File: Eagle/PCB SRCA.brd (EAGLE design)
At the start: 160 x 100 mm, 81 parts, among them IC1 DSPIC30F4011-30I_P, IC2 LM324LVIDR, IC3 LM35DZ_NOPB, IC4 FT232RL-REEL, J1 TBL002A-350-03GR-2OR, J2 TBL002A-350-03GR-2OR, J3 TBL002A-350-03GR-2OR, J4 44914-0801, J5 TBL002A-350-03GR-2OR, J6 44914-0401, Q1 TIP41C, T1 2N3904, T10 2N3904, T11 2N3904, T2 2N3904, T3 2N3904, T4 2N3904, T5 2N3904, T6 2N3904, T7 2N3904, T8 2N3904, T9 2N3904, U1 LD1117S33TR

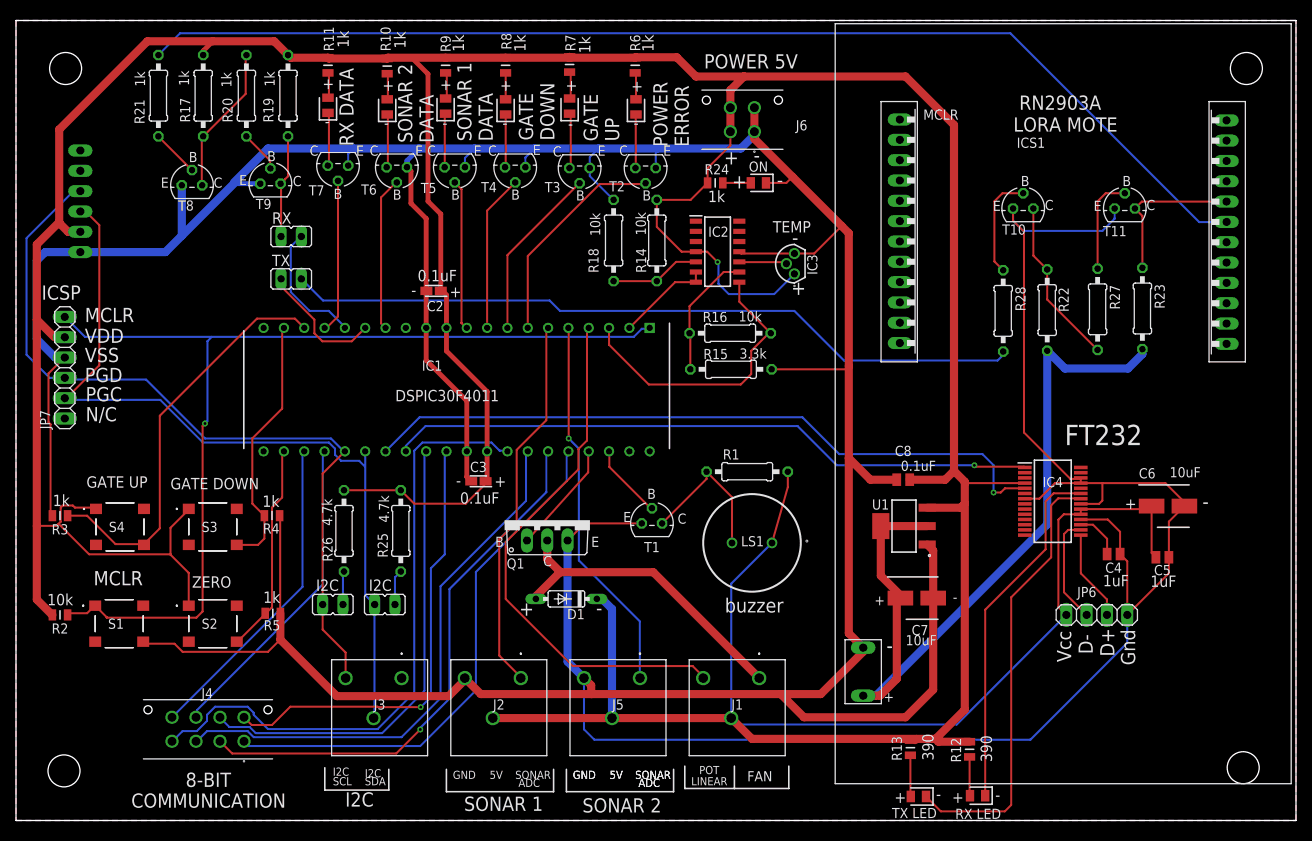
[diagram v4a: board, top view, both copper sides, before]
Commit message: 06-09-2021
se revirtio el cambio de el divisor de voltaje del lora al DSPIC
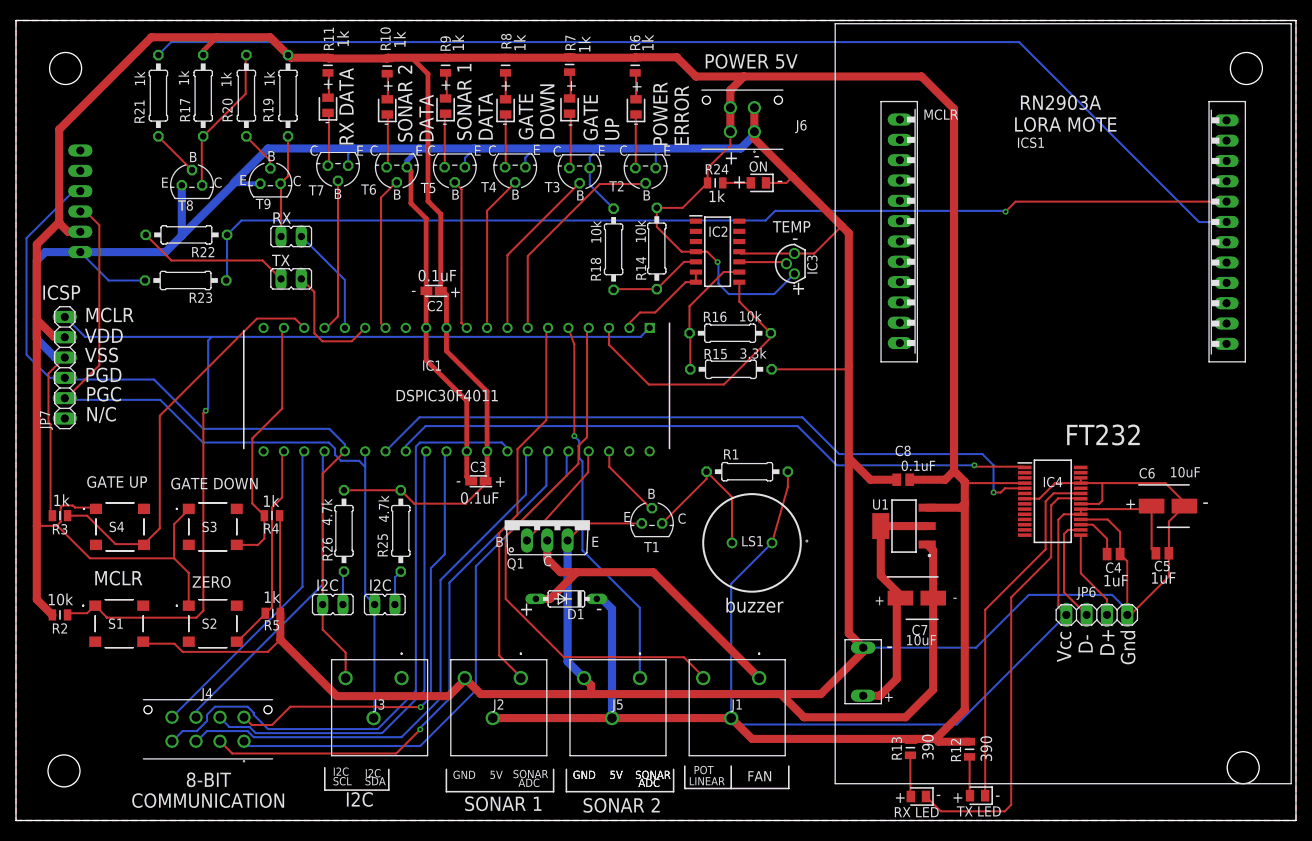
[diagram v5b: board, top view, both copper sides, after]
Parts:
- removed R27, R28: 1k, rcl:0207/10
- removed T10, T11: 2N3904, transistor-neu-to92:TO92
- R22: value 1k -> 3.3k
- R23: value 1k -> 6.8k
- moved R23 119.7 mm to (21.2, 67.5), turned to 180 degrees
- moved R22 108.0 mm to (21.3, 73.2), turned to 180 degrees
- moved R18 1.10 mm to (74.7, 71.4)
- moved R14 1.00 mm to (80.1, 71.5)
- moved C5 0.50 mm to (143.3, 33.4)
- turned JP2 to 90 degrees
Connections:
- removed net N$29: JP2.2, R28.2
- removed net N$33: R28.1, T10.2
- removed net N$34: R27.1, T11.2
- net 3.3V: no longer R22.2, R23.2
- net GND: now also R23.2; no longer T10.3, T11.3
- net N$27: now also JP2.2, R22.2; no longer R22.1, R27.2, T10.1
- net RX_LORA: now also R22.1; no longer T11.1
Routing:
- net RX_LORA: track 19.6 -> 132.5 mm, vias 0 -> 1
- net N$29: track 92.7 -> 0.00 mm
- net GND: track 698.0 -> 607.9 mm
- net 3.3V: track 98.9 -> 31.2 mm
- net N$33: track 13.1 -> 0.00 mm
- net N$34: track 12.2 -> 0.00 mm
- net RX_UART: track 16.2 -> 13.7 mm
- net FAN1: track 39.6 -> 41.5 mm
- net N$27: track 21.0 -> 19.2 mm
- net V+: track 649.5 -> 651.1 mm
- net TEMP: track 36.7 -> 35.4 mm
- net TX_UART: track 16.0 -> 14.9 mm
- net TX_LORA: track 144.4 -> 143.5 mm
- net I2C_SCL: track 99.2 -> 99.7 mm

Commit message: 06/09/2021
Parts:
- removed C8: C0805X104K1RAC3316, C0805X104K1RAC3316:CAPC2012X100N
- added C1: TAJR104K020RNJ, TAJR104K020RNJ:CAPPM2014X120N
- C3: value TAJR104K020RNJ -> C0805X104K1RAC3316; device TAJR104K020RNJ:CAPPM2014X120N -> C0805X104K1RAC3316:CAPC2012X100N
- C5: value C0805X104K1RAC3316 -> UUP1C100MCL1GS; device C0805X104K1RAC3316:CAPC2012X100N -> UUP1C100MCL1GS:CAPAE530X610N
- C6: value UUP1C100MCL1GS -> C0805X104K1RAC3316; device UUP1C100MCL1GS:CAPAE530X610N -> C0805X104K1RAC3316:CAPC2012X100N
- moved C3 86.0 mm to (143.3, 33.4)
- moved C6 33.3 mm to (110.9, 42.6), turned to 180 degrees
- moved C2 24.4 mm to (57.8, 42.4)
- moved C5 5.94 mm to (144.0, 39.3), turned to 0 degrees
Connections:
- net GND: now also C1.2, C3.1, C5.2; no longer C3.2, C5.1, C8.2
- net V+: now also C1.1, C3.2, C5.1; no longer C3.1, C5.2, C8.1
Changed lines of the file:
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@@
 <drawing>
 <settings>
-<setting alwaysvectorfont="yes"/>
+<setting alwaysvectorfont="no"/>
 <setting verticaltext="up"/>
 </settings>
@@
 <attribute name="NAME" x="87.8" y="73.6" size="1.27" layer="25" align="center"/>
 </element>
-<element name="C2" library="TAJR104K020RNJ" library_urn="urn:adsk.eagle:library:30514861" package="CAPPM2014X120N" package3d_urn="urn:adsk.eagle:package:30514864/2" value="TAJR104K020RNJ" x="52.2" y="66.2" smashed="yes" rot="R180">
+<element name="C1" library="TAJR104K020RNJ" library_urn="urn:adsk.eagle:library:30514861" package="CAPPM2014X120N" package3d_urn="urn:adsk.eagle:package:30514864/2" value="TAJR104K020RNJ" x="52.2" y="66.2" smashed="yes" rot="R180">
 <attribute name="DESCRIPTION" value="TAJ smt tant capacitor,case R,0.1uF,20V AVX 100nF SMD Solid MnO2 Tantalum Electrolytic Capacitor, 20 V dc +/-10%, TAJ Series" x="52.2" y="66.2" size="1.778" layer="27" rot="R180" display="off"/>
 <attribute name="HEIGHT" value="1.2mm" x="52.2" y="66.2" size="1.778" layer="27" rot="R180" display="off"/>
@@
 <attribute name="NAME" x="52.4" y="64.3" size="1.27" layer="25" rot="R180" align="center"/>
 </element>
-<element name="C3" library="TAJR104K020RNJ" library_urn="urn:adsk.eagle:library:30514861" package="CAPPM2014X120N" package3d_urn="urn:adsk.eagle:package:30514864/2" value="TAJR104K020RNJ" x="57.8" y="42.4" smashed="yes" rot="R180">
+<element name="C2" library="TAJR104K020RNJ" library_urn="urn:adsk.eagle:library:30514861" package="CAPPM2014X120N" package3d_urn="urn:adsk.eagle:package:30514864/2" value="TAJR104K020RNJ" x="57.8" y="42.4" smashed="yes" rot="R180">
 <attribute name="DESCRIPTION" value="TAJ smt tant capacitor,case R,0.1uF,20V AVX 100nF SMD Solid MnO2 Tantalum Electrolytic Capacitor, 20 V dc +/-10%, TAJ Series" x="57.8" y="42.4" size="1.778" layer="27" rot="R180" display="off"/>
 <attribute name="HEIGHT" value="1.2mm" x="57.8" y="42.4" size="1.778" layer="27" rot="R180" display="off"/>
@@
 <attribute name="VALUE" x="39.535" y="36.8394" size="1.27" layer="25" ratio="10" rot="R90"/>
 </element>
-<element name="C5" library="C0805X104K1RAC3316" library_urn="urn:adsk.eagle:library:30534331" package="CAPC2012X100N" package3d_urn="urn:adsk.eagle:package:30534334/2" value="C0805X104K1RAC3316" x="143.3" y="33.4" smashed="yes" rot="R180">
+<element name="C3" library="C0805X104K1RAC3316" library_urn="urn:adsk.eagle:library:30534331" package="CAPC2012X100N" package3d_urn="urn:adsk.eagle:package:30534334/2" value="C0805X104K1RAC3316" x="143.3" y="33.4" smashed="yes" rot="R180">
 <attribute name="DESCRIPTION" value="Multilayer Ceramic Capacitors MLCC - SMD/SMT 100V .1uF X7R AUTO 5mm Flex VW80808" x="143.3" y="33.4" size="1.778" layer="27" rot="R180" display="off"/>
 <attribute name="HEIGHT" value="1mm" x="143.3" y="33.4" size="1.778" layer="27" rot="R180" display="off"/>
@@
 <attribute name="NAME" x="129.6" y="42.3" size="1.27" layer="25" align="center"/>
 </element>
-<element name="C6" library="UUP1C100MCL1GS" library_urn="urn:adsk.eagle:library:30514850" package="CAPAE530X610N" package3d_urn="urn:adsk.eagle:package:30514853/2" value="UUP1C100MCL1GS" x="144" y="39.3" smashed="yes">
+<element name="C5" library="UUP1C100MCL1GS" library_urn="urn:adsk.eagle:library:30514850" package="CAPAE530X610N" package3d_urn="urn:adsk.eagle:package:30514853/2" value="UUP1C100MCL1GS" x="144" y="39.3" smashed="yes">
 <attribute name="DESCRIPTION" value="Aluminum Electrolytic Capacitors - SMD 16volts 10uF AEC-Q200" x="144" y="39.3" size="1.778" layer="27" display="off"/>
 <attribute name="HEIGHT" value="6.1mm" x="144" y="39.3" size="1.778" layer="27" display="off"/>
@@
 <attribute name="NAME" x="113" y="23.8" size="1.27" layer="25" align="center"/>
 </element>
-<element name="C8" library="C0805X104K1RAC3316" library_urn="urn:adsk.eagle:library:30534331" package="CAPC2012X100N" package3d_urn="urn:adsk.eagle:package:30534334/2" value="C0805X104K1RAC3316" x="110.9" y="42.6" smashed="yes" rot="R180">
+<element name="C6" library="C0805X104K1RAC3316" library_urn="urn:adsk.eagle:library:30534331" package="CAPC2012X100N" package3d_urn="urn:adsk.eagle:package:30534334/2" value="C0805X104K1RAC3316" x="110.9" y="42.6" smashed="yes" rot="R180">
 <attribute name="DESCRIPTION" value="Multilayer Ceramic Capacitors MLCC - SMD/SMT 100V .1uF X7R AUTO 5mm Flex VW80808" x="110.9" y="42.6" size="1.778" layer="27" rot="R180" display="off"/>
 <attribute name="HEIGHT" value="1mm" x="110.9" y="42.6" size="1.778" layer="27" rot="R180" display="off"/>
@@
 <attribute name="POPULARITY" value="81" x="21.3" y="73.2" size="1.778" layer="27" rot="R180" display="off"/>
 <attribute name="SPICEPREFIX" value="R" x="21.3" y="73.2" size="1.778" layer="27" rot="R180" display="off"/>
-<attribute name="VALUE" x="20.5606" y="71.635" size="1.27" layer="27" ratio="10" rot="R180"/>
+<attribute name="VALUE" x="20.5606" y="71.635" size="1.27" layer="25" ratio="10" rot="R180"/>
 </element>
 <element name="R23" library="rcl" library_urn="urn:adsk.eagle:library:334" package="0207/10" package3d_urn="urn:adsk.eagle:package:23491/2" value="6.8k" x="21.2" y="67.5" smashed="yes" rot="R180">
@@
 <attribute name="POPULARITY" value="81" x="21.2" y="67.5" size="1.778" layer="27" rot="R180" display="off"/>
 <attribute name="SPICEPREFIX" value="R" x="21.2" y="67.5" size="1.778" layer="27" rot="R180" display="off"/>
-<attribute name="VALUE" x="20.4606" y="66.035" size="1.27" layer="27" ratio="10" rot="R180"/>
+<attribute name="VALUE" x="20.4606" y="66.035" size="1.27" layer="25" ratio="10" rot="R180"/>
 </element>
 </elements>
@@
 <contactref element="R4" pad="1"/>
 <contactref element="R3" pad="1"/>
+<contactref element="C1" pad="2"/>
 <contactref element="C2" pad="2"/>
-<contactref element="C3" pad="2"/>
 <contactref element="IC1" pad="31"/>
 <wire x1="51.27" y1="61.575" x2="51.27" y2="66.04" width="0.6096" layer="1"/>
@@
 <contactref element="IC2" pad="11"/>
 <contactref element="R18" pad="1"/>
-<contactref element="C5" pad="1"/>
+<contactref element="C3" pad="1"/>
 <contactref element="C4" pad="1"/>
 <contactref element="IC4" pad="7"/>
@@
 <contactref element="IC4" pad="25"/>
 <contactref element="IC4" pad="26"/>
-<contactref element="C6" pad="2"/>
+<contactref element="C5" pad="2"/>
 <contactref element="S1" pad="D1"/>
 <contactref element="J6" pad="3"/>
@@
 <vertex x="160" y="100"/>
 </polygon>
-<contactref element="C8" pad="2"/>
+<contactref element="C6" pad="2"/>
 <contactref element="C7" pad="2"/>
 <contactref element="U1" pad="1"/>
@@
 <contactref element="S2" pad="A1"/>
 <contactref element="IC1" pad="11"/>
+<contactref element="C1" pad="1"/>
 <contactref element="C2" pad="1"/>
-<contactref element="C3" pad="1"/>
 <wire x1="53.1" y1="75.8" x2="53.1" y2="66.4" width="0.6096" layer="1"/>
 <wire x1="53.81" y1="61.575" x2="53.81" y2="65.69" width="0.6096" layer="1"/>
@@
 <wire x1="19.766" y1="37.038" x2="19.766" y2="32.774" width="0.254" layer="1"/>
 <contactref element="U1" pad="3"/>
-<contactref element="C8" pad="1"/>
+<contactref element="C6" pad="1"/>
 <wire x1="118.6" y1="13.85" x2="118.6" y2="39.6" width="1.016" layer="1"/>
 <wire x1="118.6" y1="39.6" x2="118.6" y2="42.175" width="1.016" layer="1"/>
@@
 <wire x1="90.2" y1="12" x2="89.4" y2="12.8" width="0.254" layer="16"/>
 <wire x1="117.59" y1="12" x2="90.2" y2="12" width="0.254" layer="16"/>
-<contactref element="C5" pad="2"/>
-<contactref element="C6" pad="1"/>
+<contactref element="C3" pad="2"/>
+<contactref element="C5" pad="1"/>
 <wire x1="118.6" y1="42.175" x2="118.6" y2="42.35" width="1.016" layer="1"/>
 <wire x1="118.6" y1="42.35" x2="117.25" y2="43.7" width="1.016" layer="1"/>

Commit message: 23-09-2021
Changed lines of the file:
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@@
 <drawing>
 <settings>
-<setting alwaysvectorfont="no"/>
+<setting alwaysvectorfont="yes"/>
 <setting verticaltext="up"/>
 </settings>
@@
 </layers>
 <board>
-<fusionsync huburn="a.YnVzaW5lc3M6Z21haWwxODU1MTgw" projecturn="a.YnVzaW5lc3M6Z21haWwxODU1MTgwIzIwMjEwODI0NDM3MjIwNDA2" f3durn="urn:adsk.wipprod:dm.lineage:9RdnEizDSZWnVXfx1H3Ocg" pcbguid="" lastpulledtime="" lastsyncedchangeguid="" latestrevisionid="20cc03f1-af99-4a4c-a276-f269cff5e179" lastsyncedrevisionid="20cc03f1-af99-4a4c-a276-f269cff5e179" lastboardhashguid="1d953e68-588c-0330-f4bb-c947bb569c06" lastpushedtime="2021-09-06T21:43:07Z" linktopcb3d="true"/>
+<fusionsync huburn="a.YnVzaW5lc3M6Z21haWwxODU1MTgw" projecturn="a.YnVzaW5lc3M6Z21haWwxODU1MTgwIzIwMjEwODI0NDM3MjIwNDA2" f3durn="urn:adsk.wipprod:dm.lineage:9RdnEizDSZWnVXfx1H3Ocg" pcbguid="" lastpulledtime="" lastsyncedchangeguid="" latestrevisionid="c4a1ce47-2d88-4aa0-bed6-f5c6ff134eef" lastsyncedrevisionid="c4a1ce47-2d88-4aa0-bed6-f5c6ff134eef" lastboardhashguid="45040a8e-f6d4-4a60-a59d-9d538ec767cb" lastpushedtime="2021-09-06T22:51:12Z" linktopcb3d="true"/>
 <plain>
 <text x="9.69" y="29.4" size="1.778" layer="25">MCLR</text>
@@
 <wire x1="133.1" y1="38.275" x2="133.1" y2="38.925" width="0.254" layer="1"/>
 <wire x1="133.1" y1="38.275" x2="130.975" y2="38.275" width="0.254" layer="1"/>
-<wire x1="130.975" y1="38.275" x2="130.3" y2="37.6" width="0.254" layer="1"/>
-<wire x1="130.3" y1="37.6" x2="130.3" y2="26.69" width="0.254" layer="1"/>
-<wire x1="130.3" y1="26.69" x2="131.29" y2="25.7" width="0.254" layer="1"/>
+<wire x1="130.975" y1="38.275" x2="130.1" y2="37.4" width="0.254" layer="1"/>
+<wire x1="130.1" y1="37.4" x2="130.1" y2="26.89" width="0.254" layer="1"/>
+<wire x1="130.1" y1="26.89" x2="131.29" y2="25.7" width="0.254" layer="1"/>
 <wire x1="126.1" y1="42.175" x2="118.6" y2="42.175" width="0.254" layer="1"/>
 <wire x1="94.5" y1="34.7" x2="96.48" y2="41.68" width="0.254" layer="1"/>
@@
 <contactref element="JP6" pad="2"/>
 <contactref element="IC4" pad="16"/>
-<wire x1="133.83" y1="25.7" x2="131" y2="28.53" width="0.254" layer="1"/>
-<wire x1="131" y1="28.53" x2="131" y2="35.8" width="0.254" layer="1"/>
+<wire x1="133.83" y1="25.7" x2="133.73" y2="25.8" width="0.254" layer="1"/>
+<wire x1="133.73" y1="27.1" x2="133.73" y2="25.8" width="0.254" layer="1"/>
+<wire x1="133.73" y1="27.1" x2="131" y2="29.83" width="0.254" layer="1"/>
+<wire x1="131" y1="29.83" x2="131" y2="35.8" width="0.254" layer="1"/>
 <wire x1="131" y1="35.8" x2="131.525" y2="36.325" width="0.254" layer="1"/>
 <wire x1="131.525" y1="36.325" x2="133.1" y2="36.325" width="0.254" layer="1"/>
@@
 <contactref element="IC4" pad="23"/>
 <contactref element="LED7" pad="1"/>
-<wire x1="128.7" y1="39.9" x2="129.7" y2="40.9" width="0.254" layer="1"/>
+<wire x1="128.4" y1="39.6" x2="129.7" y2="40.9" width="0.254" layer="1"/>
 <wire x1="133.075" y1="40.9" x2="133.1" y2="40.875" width="0.254" layer="1"/>
 <wire x1="129.7" y1="40.9" x2="133.075" y2="40.9" width="0.254" layer="1"/>
 <wire x1="121.15" y1="3.1" x2="121.15" y2="26.35" width="0.254" layer="1"/>
-<wire x1="128.7" y1="33.9" x2="128.7" y2="39.9" width="0.254" layer="1"/>
-<wire x1="121.15" y1="26.35" x2="128.7" y2="33.9" width="0.254" layer="1"/>
+<wire x1="128.4" y1="33.6" x2="128.4" y2="39.6" width="0.254" layer="1"/>
+<wire x1="121.15" y1="26.35" x2="128.4" y2="33.6" width="0.254" layer="1"/>
 </signal>
 <signal name="N$18">
@@
 <wire x1="115.607" y1="1.143" x2="123.6" y2="1.143" width="0.254" layer="1"/>
 <wire x1="123.6" y1="1.143" x2="124.4" y2="1.943" width="0.254" layer="1"/>
-<wire x1="124.4" y1="27.9" x2="129.4" y2="32.9" width="0.254" layer="1"/>
-<wire x1="129.4" y1="32.9" x2="129.4" y2="39.4" width="0.254" layer="1"/>
-<wire x1="129.4" y1="39.4" x2="130.269" y2="40.269" width="0.254" layer="1"/>
+<wire x1="124.4" y1="27.9" x2="129.2" y2="32.7" width="0.254" layer="1"/>
+<wire x1="129.2" y1="32.7" x2="129.2" y2="39.2" width="0.254" layer="1"/>
+<wire x1="129.2" y1="39.2" x2="130.269" y2="40.269" width="0.254" layer="1"/>
 <wire x1="133.056" y1="40.269" x2="133.1" y2="40.225" width="0.254" layer="1"/>
 <wire x1="124.4" y1="1.943" x2="124.4" y2="27.9" width="0.254" layer="1"/>
